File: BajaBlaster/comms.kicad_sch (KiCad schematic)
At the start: 1 part, among them J2 Conn_01x06_Pin

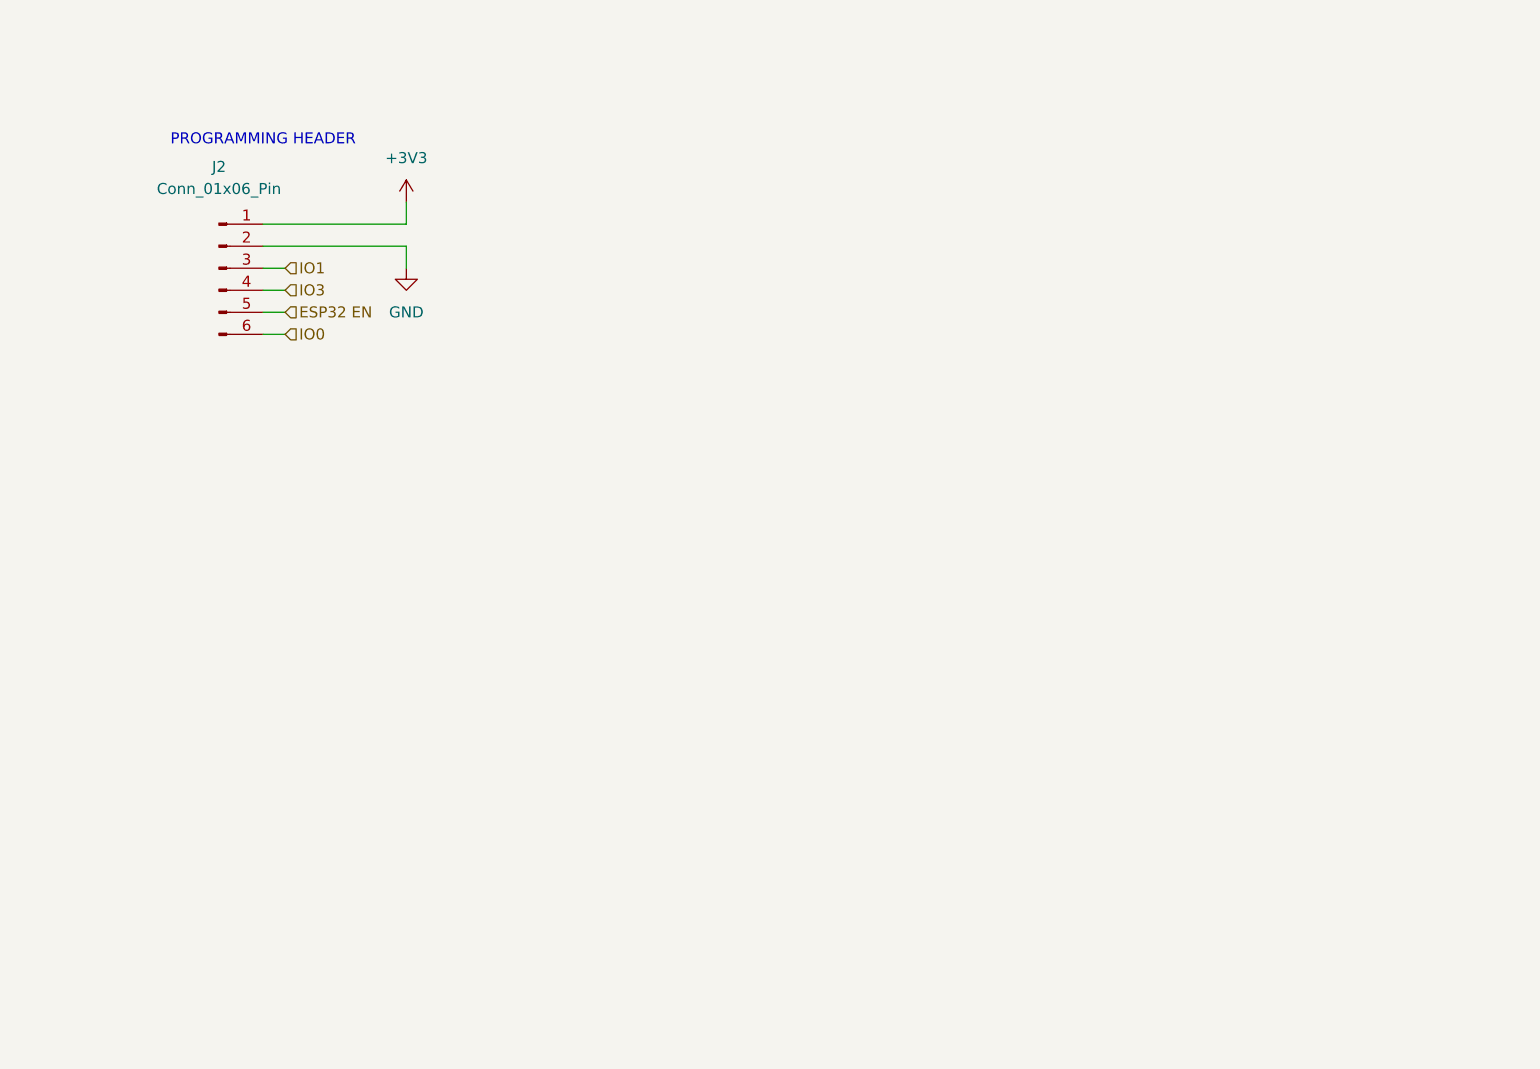
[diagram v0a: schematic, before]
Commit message: added the cam bus and started setting up master slave arch
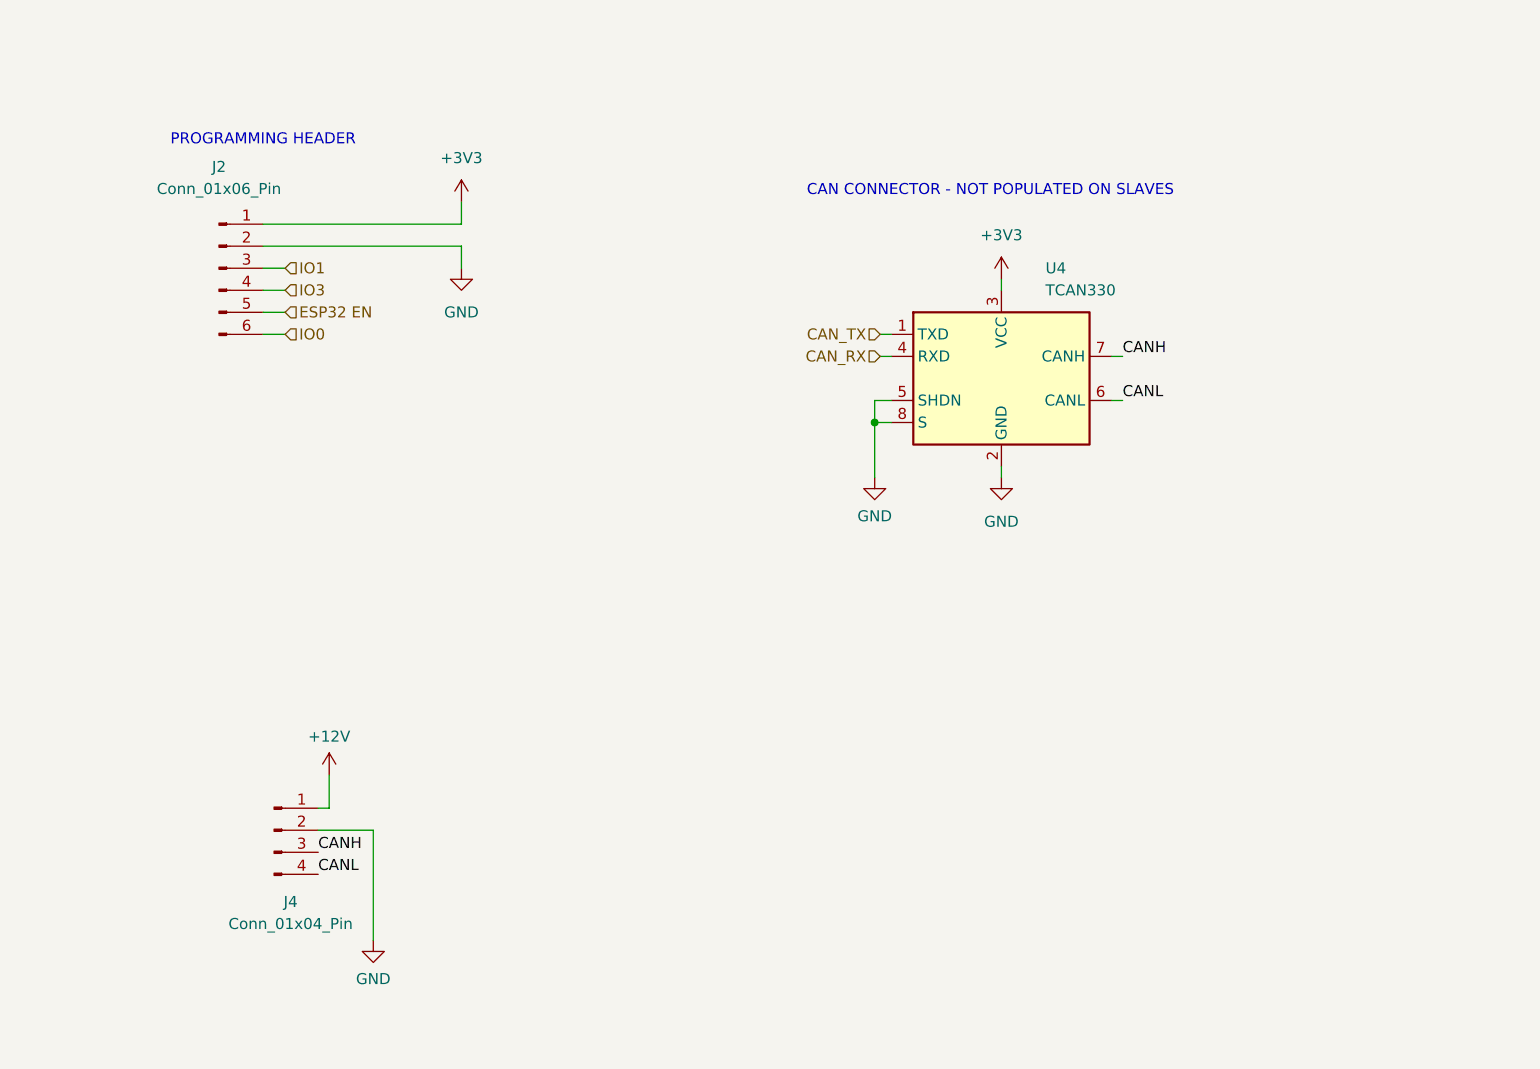
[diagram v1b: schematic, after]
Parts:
- added J4: Conn_01x04_Pin, symbol Connector:Conn_01x04_Pin
- added U4: TCAN330, symbol Interface_CAN_LIN:TCAN330
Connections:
- net +3V3: now also U4.3 (VCC)
- net GND: now also J4.2 (Pin_2), U4.2 (GND), U4.5 (SHDN), U4.8 (S)
- new net +12V: J4.1 (Pin_1)
- new net CANH: J4.3 (Pin_3), U4.7 (CANH)
- new net CANL: J4.4 (Pin_4), U4.6 (CANL)
- new net CAN_RX: U4.4 (RXD)
- new net CAN_TX: U4.1 (TXD)
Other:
- note added: "CAN CONNECTOR - NOT POPULATED ON SLAVES"

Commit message: added new h tags
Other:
- note added: "CAN TRANSCEIVER"
- moved on the sheet: J4, U4

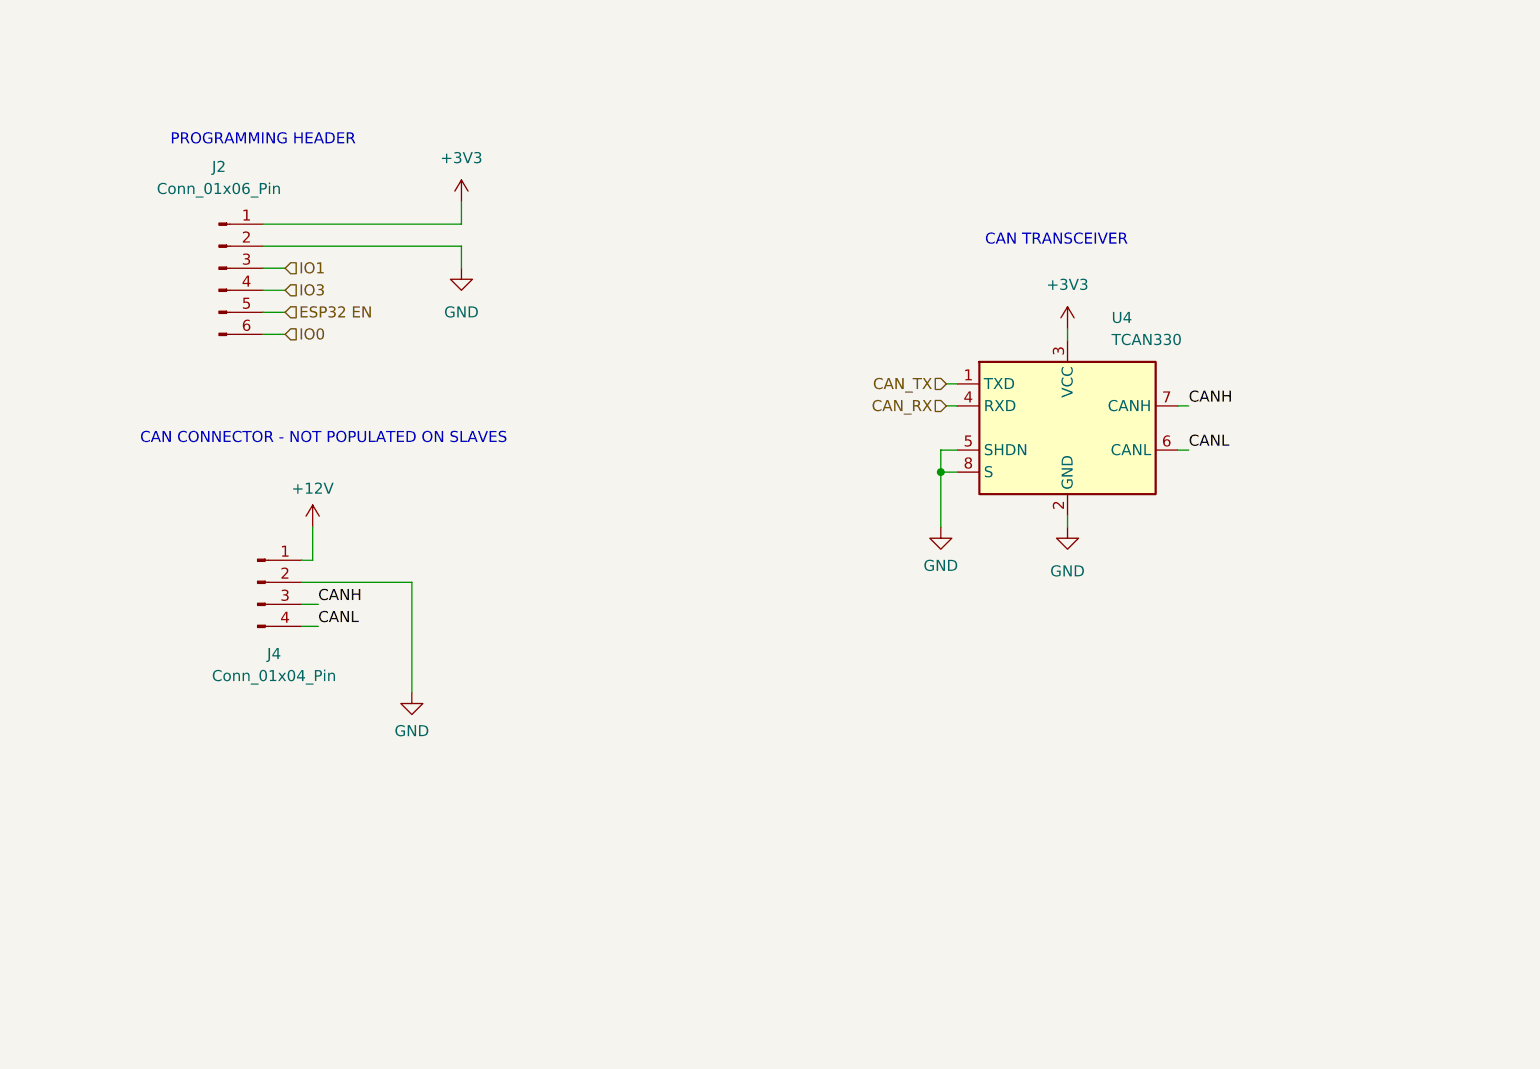
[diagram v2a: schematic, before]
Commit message: added wiring for interconnect and finished can bus wiring
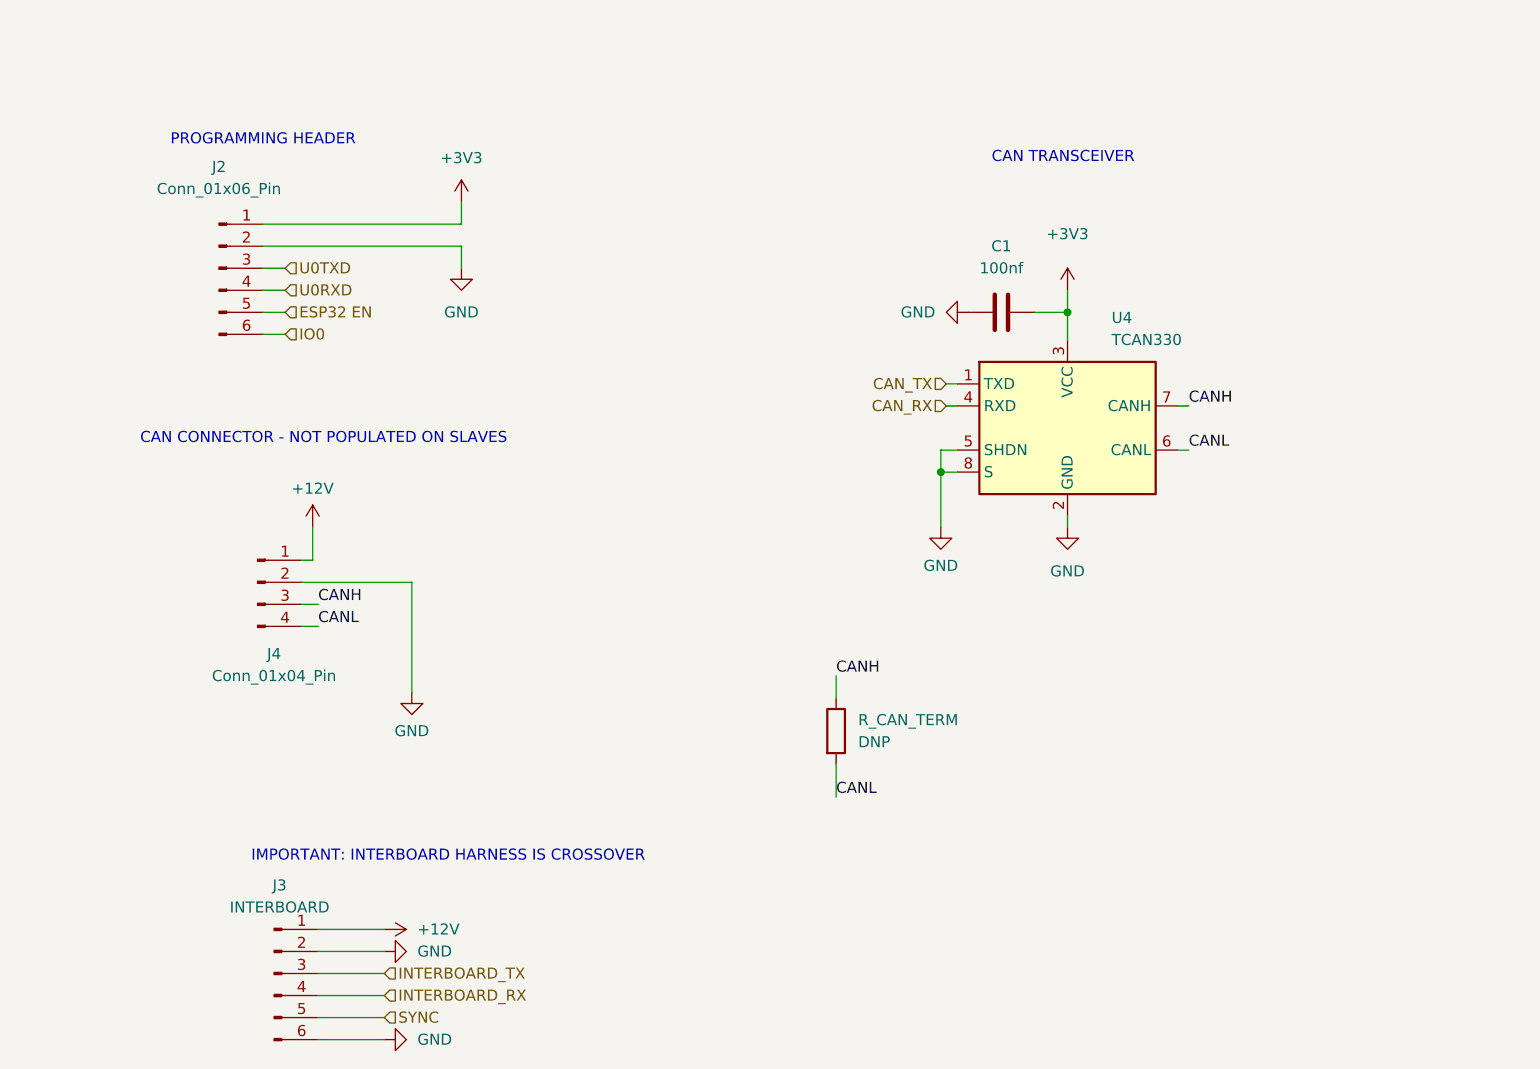
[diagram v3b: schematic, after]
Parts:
- added C1: 100nf, symbol Device:C
- added J3: INTERBOARD, Package_DFN_QFN:QFN-20-1EP_5x5mm_P0.65mm_EP3.35x3.35mm, symbol Connector:Conn_01x06_Pin
- added R_CAN_TERM: DNP, symbol Device:R
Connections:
- net +12V: now also J3.1 (Pin_1)
- net +3V3: now also C1.2
- net CANH: now also R_CAN_TERM.1
- net CANL: now also R_CAN_TERM.2
- net GND: now also C1.1, J3.2 (Pin_2), J3.6 (Pin_6)
- net IO1 renamed U0TXD
- net IO3 renamed U0RXD
- new net INTERBOARD_RX: J3.4 (Pin_4)
- new net INTERBOARD_TX: J3.3 (Pin_3)
- new net SYNC: J3.5 (Pin_5)
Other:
- note added: "IMPORTANT: INTERBOARD HARNESS IS CROSSOVER"

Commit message: doing lots of small tweaks and fixups
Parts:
- renumbered C1 to C501, J2 to J501, J3 to J502, J4 to J503, R_CAN_TERM to R_CAN_TERM501, U4 to U501
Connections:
- net ESP32 EN renamed ESP32_EN
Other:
- note added: "CAN CONNECTOR"
- note added: "INTERBOARD HARNESS IS CROSSOVER"
- note removed: "CAN CONNECTOR - NOT POPULATED ON SLAVES"
- note removed: "IMPORTANT: INTERBOARD HARNESS IS CROSSOVER"
- title: (none) -> COMMS_REV_A
- moved on the sheet: C501, J501, J502, J503, R_CAN_TERM501, U501

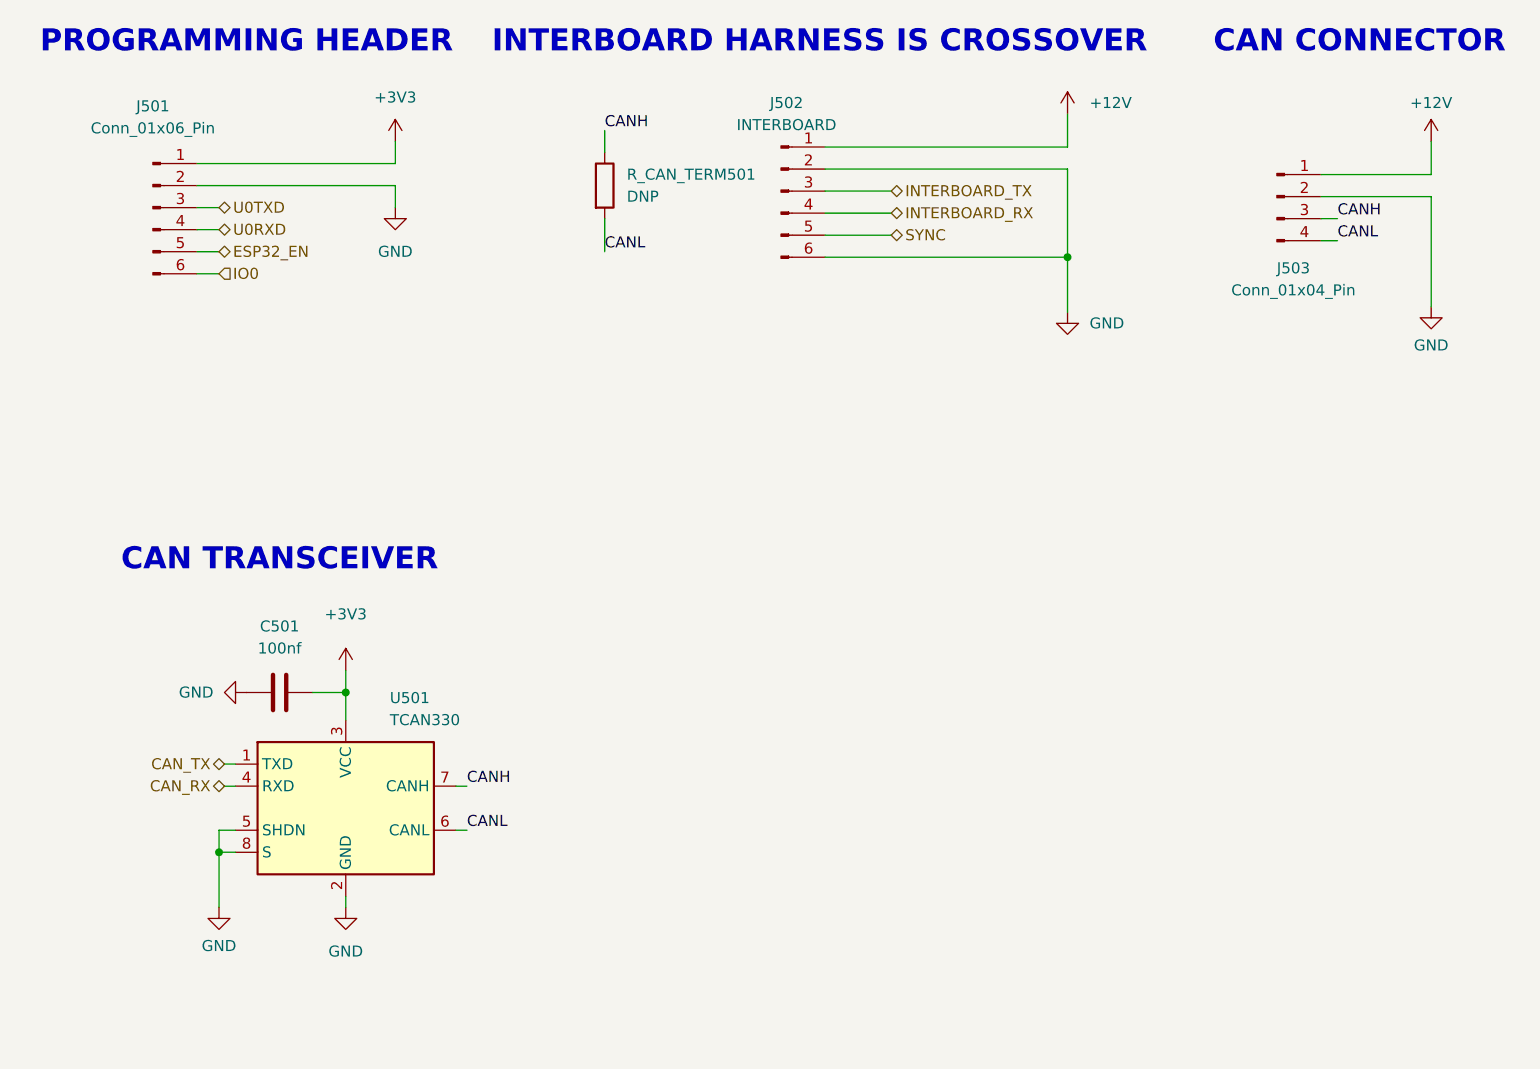
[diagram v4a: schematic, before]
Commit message: added better formatting across schematic
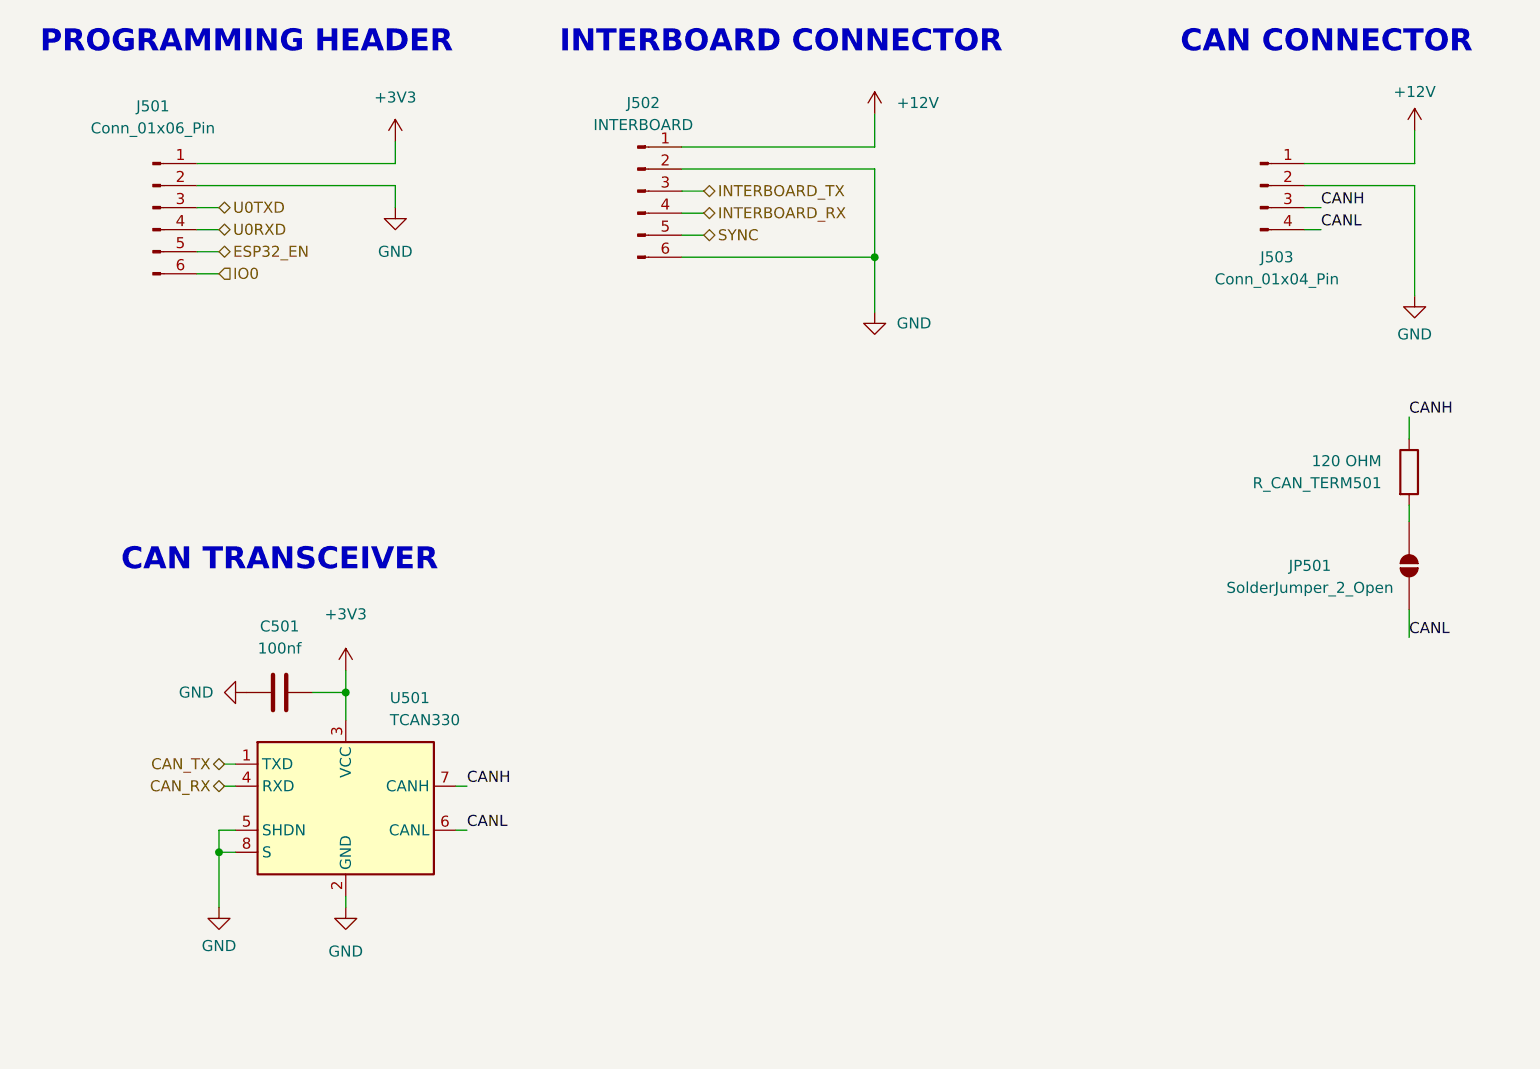
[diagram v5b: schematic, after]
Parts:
- added JP501: SolderJumper_2_Open, symbol Jumper:SolderJumper_2_Open
- R_CAN_TERM501: value DNP -> 120 OHM
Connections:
- net CANL: now also JP501.2 (B); no longer R_CAN_TERM501.2
- new net: JP501.1 (A), R_CAN_TERM501.2
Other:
- note added: "INTERBOARD CONNECTOR"
- note removed: "INTERBOARD HARNESS IS CROSSOVER"
- company: (none) -> Olin Baja SAE
- title: COMMS_REV_A -> BAJA_BLASTER
- moved on the sheet: J502, J503, R_CAN_TERM501
